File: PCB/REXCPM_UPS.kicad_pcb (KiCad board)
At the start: 2 copper layers, 51.3 x 18.3 mm, 7 parts, among them J1 Model_100_System_BUS, J2 Conn_01x03_Pin, U1 7402

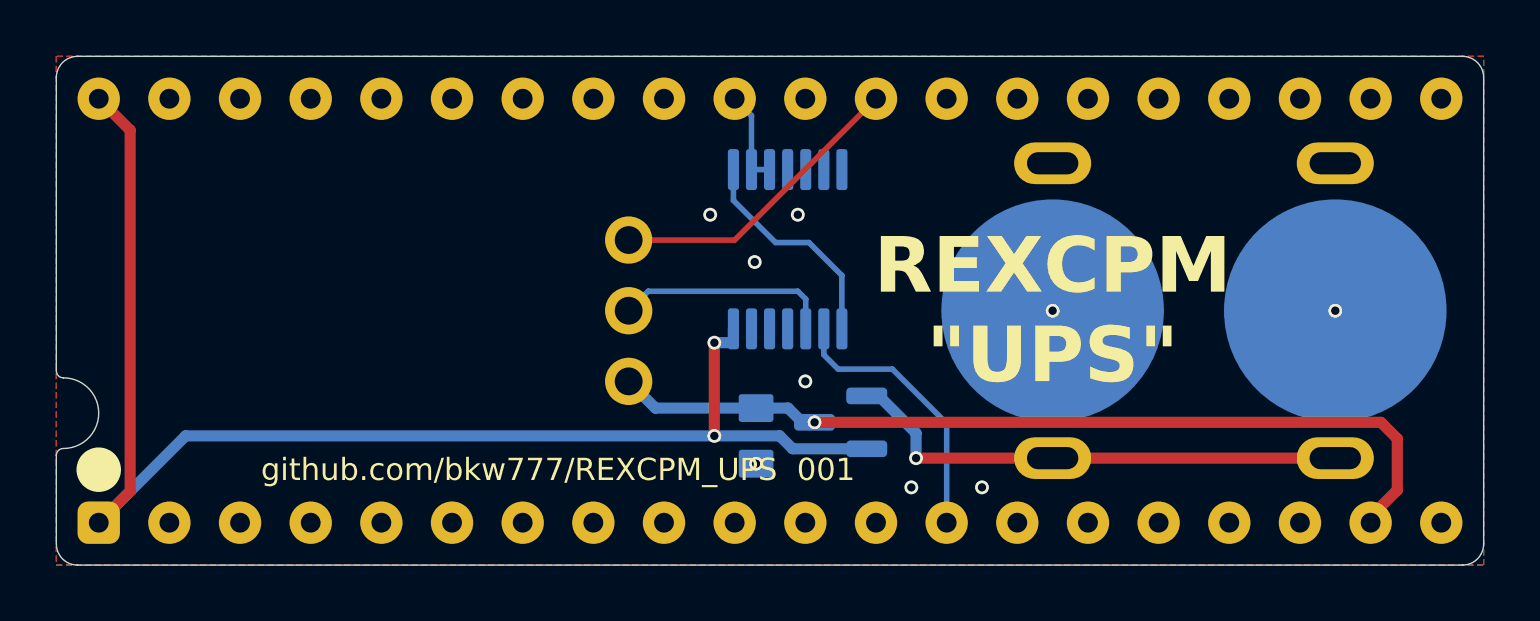
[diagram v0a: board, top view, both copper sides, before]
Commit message: replace 7402 with 742g02
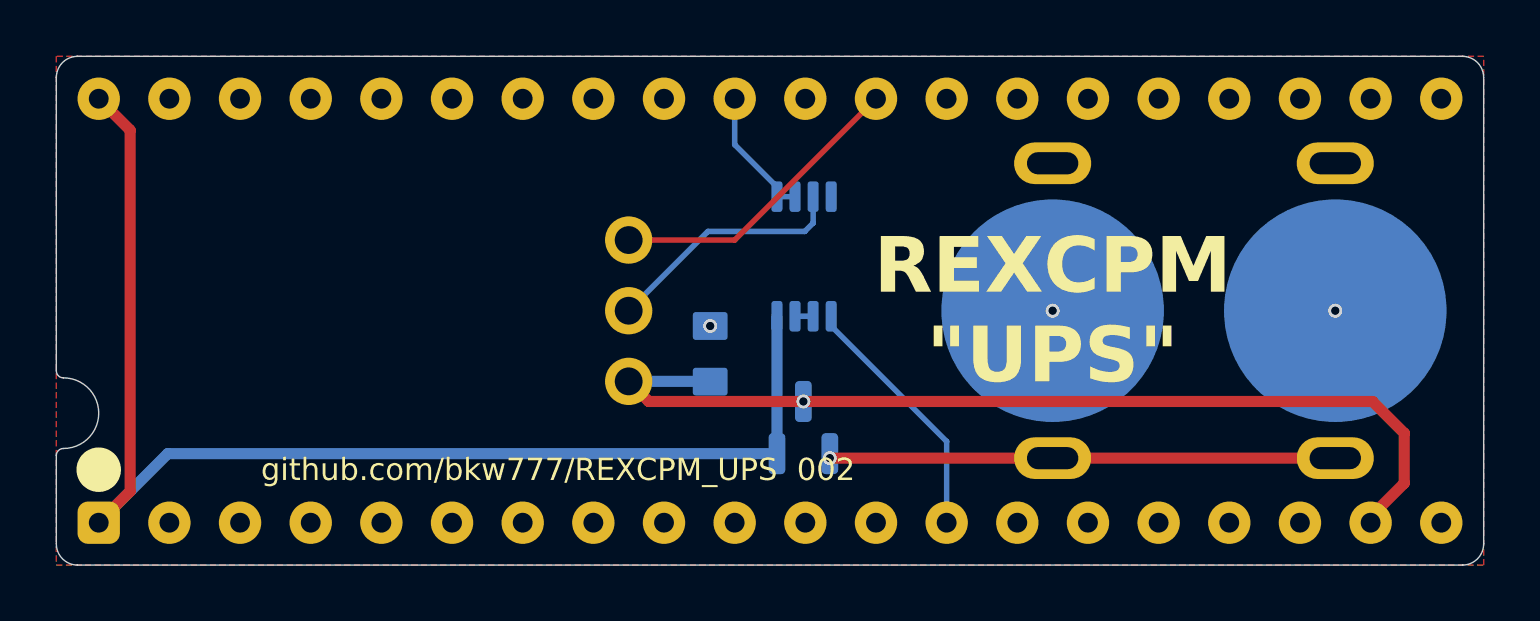
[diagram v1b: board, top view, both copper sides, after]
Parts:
- BT1: value Keystone_3031 -> BAT_3031
- U1: value 7402 -> 742G02; footprint 000_LOCAL:TSSOP-14_4.4x5mm_P0.65mm -> 000_LOCAL:TSSOP-8_3x3mm_P0.65mm
- moved C1 3.38 mm to (134.4, 106.3), turned to 90 degrees
- moved D1 1.35 mm to (137.7, 109.0), turned to 90 degrees
- moved U1 0.64 mm to (137.8, 102.8)
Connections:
- U1 pad 1: Net-(U1-Pad1) -> /A15
- U1 pad 3: /A15 -> /RAM
- U1 pad 4: unconnected-(U1-Pad4) -> GND
- U1 pad 5: GND -> /IO/~{M}
- U1 pad 6: GND -> Net-(U1-Pad6)
- U1 pad 7: GND -> Net-(U1-Pad6)
- U1 pad 8: Net-(U1-Pad1) -> VBUS
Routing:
- net Net-(U1-Pad1): track 8.04 -> 0.00 mm
- net /RAM_RST: track 31.9 -> 35.3 mm
- net VBUS: track 49.8 -> 46.5 mm, vias 2 -> 0
- net /A15: track 3.45 -> 4.80 mm
- net /RAM: track 7.84 -> 8.88 mm
- net /IO/~{M}: track 9.94 -> 9.14 mm
- net Net-(U1-Pad6): track 0.00 -> 0.65 mm
- net GND: vias 9 -> 3
